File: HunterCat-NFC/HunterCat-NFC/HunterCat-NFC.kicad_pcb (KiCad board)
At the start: 2 copper layers, 80.7 x 33.5 mm, 71 parts, among them J1 Battery, J2 Conn_01x06_Female, P1 USB_C_Plug_USB2.0, Q1 DMG3415U-7, SW1 RESET, SW2 GPIO, SW3 GPIO1, SW4 GPIO2, SW5 ON, U1 ATSAMD21E18A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

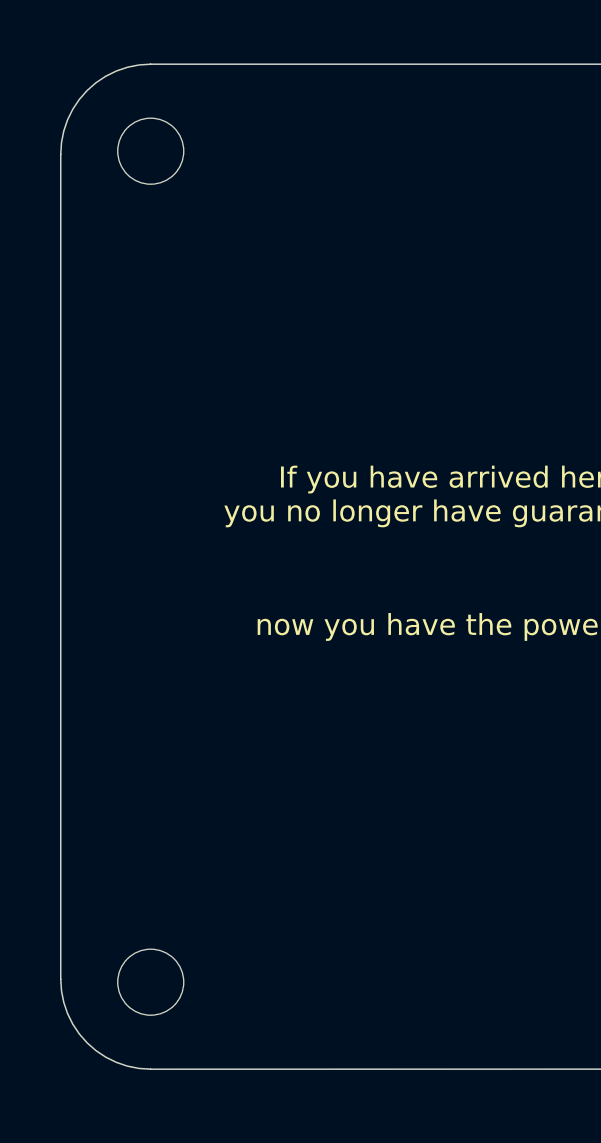
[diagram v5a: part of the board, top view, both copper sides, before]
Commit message: Moved footprints
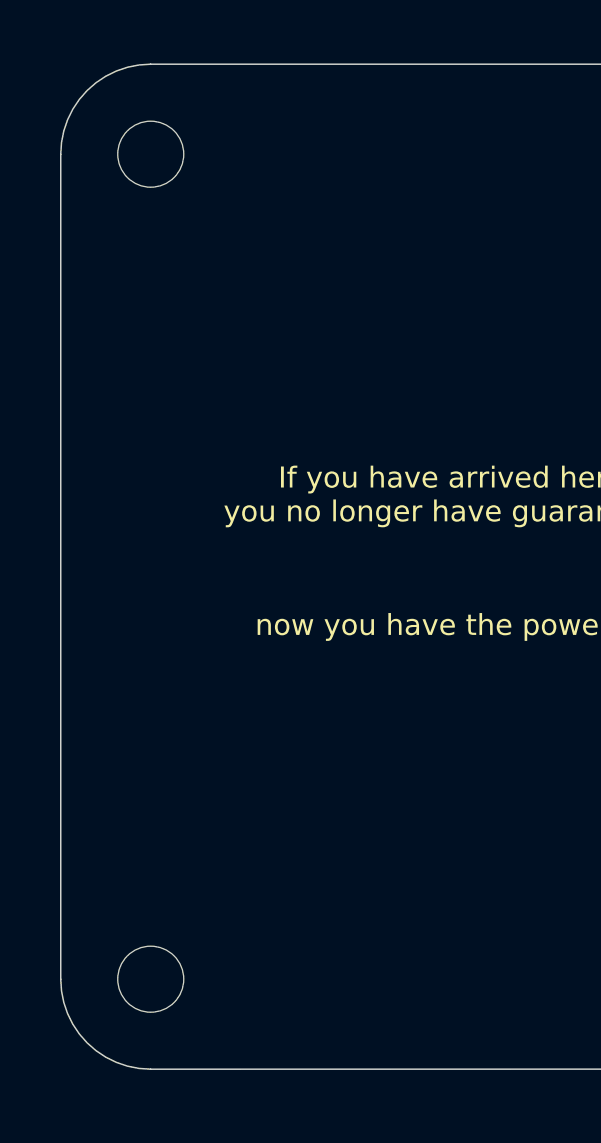
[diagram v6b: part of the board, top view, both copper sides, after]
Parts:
- moved H1 0.10 mm to (83.0, 78.5)
- moved H2 0.10 mm to (83.0, 106.0)
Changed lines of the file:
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@@
   )
   (setup
-    (last_trace_width 0.5)
+    (last_trace_width 0.35)
     (user_trace_width 0.2)
     (user_trace_width 0.25)
@@
   )
   (module MountingHole:MountingHole_2.2mm_M2 (layer F.Cu)
-    (at 83 106.1)
+    (at 83 106)
     (descr "Mounting Hole 2.2mm, no annular, M2")
     (tags "mounting hole 2.2mm no annular m2")
@@
   )
   (module MountingHole:MountingHole_2.2mm_M2 (layer F.Cu)
-    (at 83 78.4)
+    (at 83 78.5)
     (descr "Mounting Hole 2.2mm, no annular, M2")
     (tags "mounting hole 2.2mm no annular m2")

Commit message: update v1.2 footprint
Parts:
- C14: value 56pF/50V -> 100pF/50V
- C18: value 56pF -> 100pF/50V
- R19, R20: value 100k -> 100K
- U5: footprint USON:USON-8 -> hunter-cat-nfc:PSON50P200X300X50-9N
- moved U5 1.22 mm to (120.1, 89.2)
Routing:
- net /CS: track 8.21 -> 17.6 mm, vias 2 -> 0
- net +3V3: track 130.6 -> 133.7 mm
- net /MISO: track 3.56 -> 4.47 mm
- net /CLK: track 13.8 -> 14.3 mm
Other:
- board text added: "V1.2"
- board text removed: "V1.1"
